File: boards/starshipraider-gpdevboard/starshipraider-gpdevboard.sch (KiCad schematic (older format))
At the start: 68 parts, among them J1 STARSHIPRAIDER_IOBOARD_MODULE, J2 GREENPAK_DEVKIT_HDR, P1 MMCX, P2 MMCX, P3 CONN_01X02, U1 74LVC1T45, U10 74LVC1T45, U11 74LVC1T45, U12 74LVC1T45, U13 74LVC1T45, U14 74LVC1T45, U15 74LVC1T45, U16 74LVC1T45, U17 74LVC1T45, U18 74LVC1T45, U19 TCA6424A, U2 74LVC1T45, U3 74LVC1T45, U4 74LVC1T45, U5 74LVC1T45, U6 74LVC1T45, U7 74LVC1T45, U8 74LVC1T45, U9 74LVC1T45

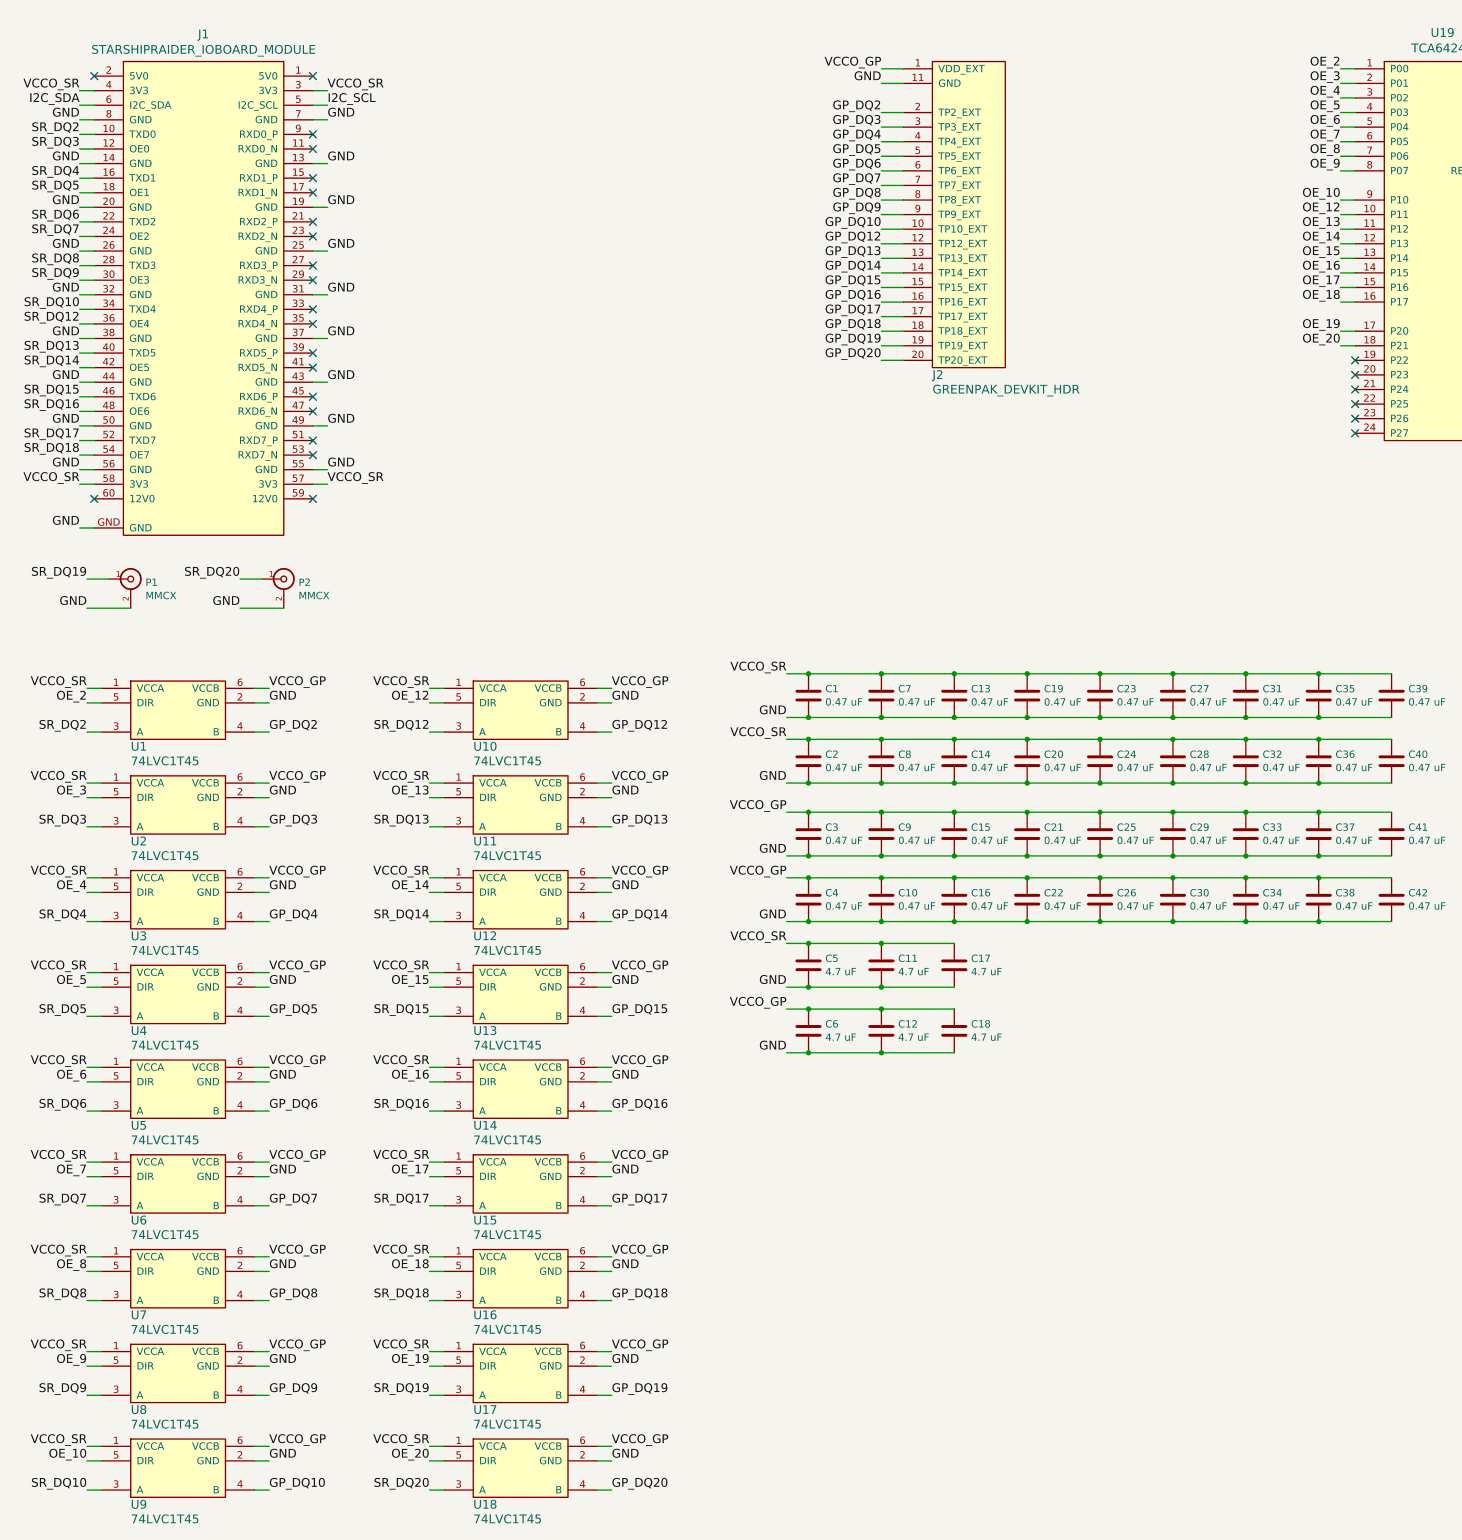
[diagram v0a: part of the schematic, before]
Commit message: Updating file: starshipraider-gpdevboard.kicad_pcb with current completely routed design
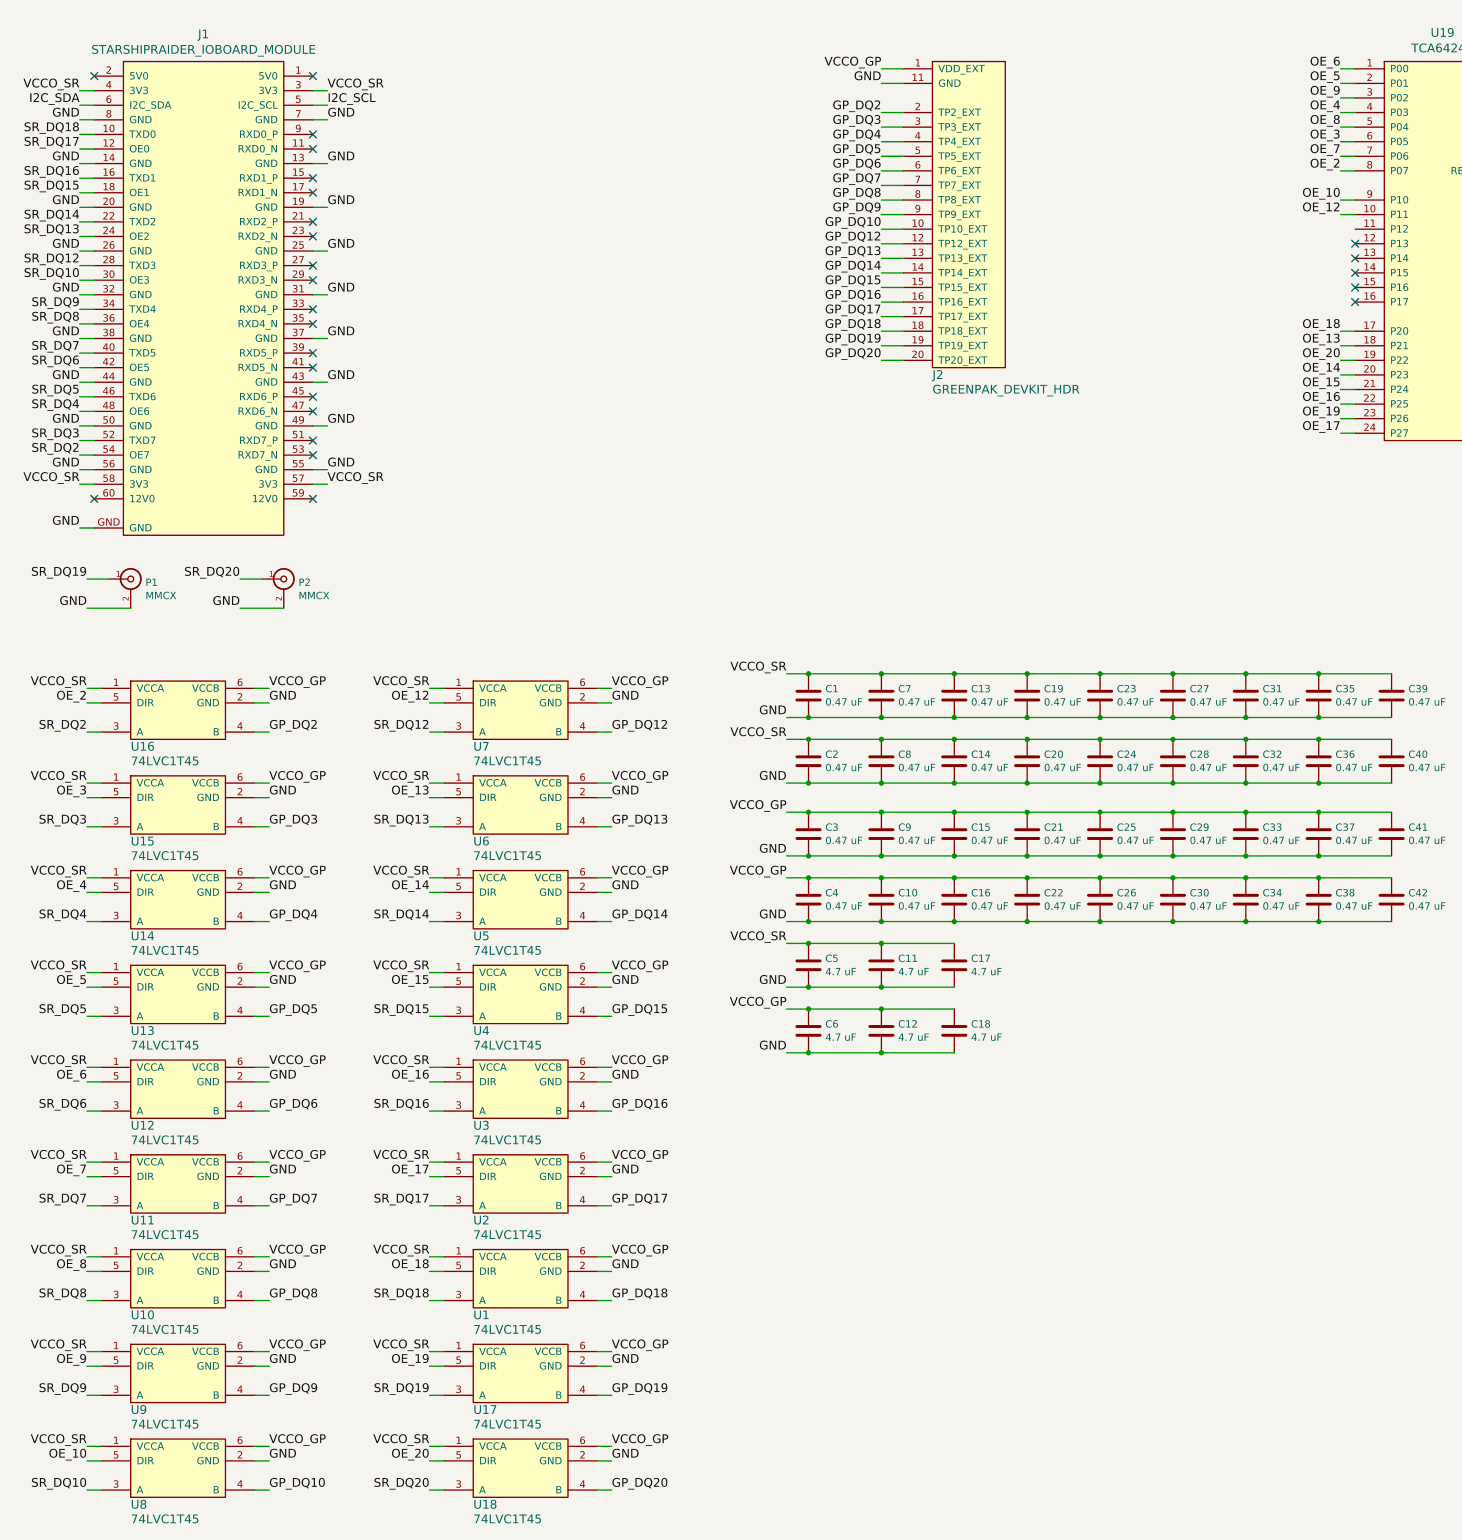
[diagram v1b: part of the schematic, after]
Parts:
- C1, C10, C13, C14, C15, C16, C19, C2, C20, C21, C22, C23, C24, C25, C26, C27, C28, C29, C3, C30, C31, C32, C33, C34, C35, C36, C37, C38, C39, C4, C40, C41, C42, C43, C7, C8, C9: footprint (none) -> azonenberg_pcb:EIA_0402_CAP_NOSILK
- C11, C12, C17, C18, C5, C6: footprint (none) -> azonenberg_pcb:EIA_0603_CAP_NOSILK
- J1: footprint (none) -> azonenberg_pcb:CONN_SAMTEC_QSH-030-01-L-D-A
- J2: footprint (none) -> azonenberg_pcb:CONN_HEADER_2.54MM_2x10_RA_FEMALE
- P1, P2: footprint (none) -> azonenberg_pcb:CONN_MMCX_LINX_CONNMMCX002SMD
- P3: footprint (none) -> azonenberg_pcb:CONN_HEADER_2.54MM_1x2
- R1: footprint (none) -> azonenberg_pcb:EIA_0402_RES_NOSILK
- U1, U10, U11, U12, U13, U14, U15, U16, U17, U18, U2, U3, U4, U5, U6, U7, U8, U9: footprint (none) -> azonenberg_pcb:SOT23_6
- U19: footprint (none) -> azonenberg_pcb:QFN_32_0.5MM_5x5MM
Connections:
- net GP_DQ10: now also U8.4 (B); no longer U9.4 (B)
- net GP_DQ12: now also U7.4 (B); no longer U10.4 (B)
- net GP_DQ13: now also U6.4 (B); no longer U11.4 (B)
- net GP_DQ14: now also U5.4 (B); no longer U12.4 (B)
- net GP_DQ15: now also U4.4 (B); no longer U13.4 (B)
- net GP_DQ16: now also U3.4 (B); no longer U14.4 (B)
- net GP_DQ17: now also U2.4 (B); no longer U15.4 (B)
- net GP_DQ18: now also U1.4 (B); no longer U16.4 (B)
- net GP_DQ2: now also U16.4 (B); no longer U1.4 (B)
- net GP_DQ3: now also U15.4 (B); no longer U2.4 (B)
- net GP_DQ4: now also U14.4 (B); no longer U3.4 (B)
- net GP_DQ5: now also U13.4 (B); no longer U4.4 (B)
- net GP_DQ6: now also U12.4 (B); no longer U5.4 (B)
- net GP_DQ7: now also U11.4 (B); no longer U6.4 (B)
- net GP_DQ8: now also U10.4 (B); no longer U7.4 (B)
- net GP_DQ9: now also U9.4 (B); no longer U8.4 (B)
- net OE_10: now also U8.5 (DIR); no longer U9.5 (DIR)
- net OE_12: now also U7.5 (DIR); no longer U10.5 (DIR)
- net OE_13: now also U19.18 (P21), U6.5 (DIR); no longer U11.5 (DIR), U19.11 (P12)
- net OE_14: now also U19.20 (P23), U5.5 (DIR); no longer U12.5 (DIR), U19.12 (P13)
- net OE_15: now also U19.21 (P24), U4.5 (DIR); no longer U13.5 (DIR), U19.13 (P14)
- net OE_16: now also U19.22 (P25), U3.5 (DIR); no longer U14.5 (DIR), U19.14 (P15)
- net OE_17: now also U19.24 (P27), U2.5 (DIR); no longer U15.5 (DIR), U19.15 (P16)
- net OE_18: now also U1.5 (DIR), U19.17 (P20); no longer U16.5 (DIR), U19.16 (P17)
- net OE_19: now also U19.23 (P26); no longer U19.17 (P20)
- net OE_2: now also U16.5 (DIR), U19.8 (P07); no longer U1.5 (DIR), U19.1 (P00)
- net OE_20: now also U19.19 (P22); no longer U19.18 (P21)
- net OE_3: now also U15.5 (DIR), U19.6 (P05); no longer U19.2 (P01), U2.5 (DIR)
- net OE_4: now also U14.5 (DIR), U19.4 (P03); no longer U19.3 (P02), U3.5 (DIR)
- net OE_5: now also U13.5 (DIR), U19.2 (P01); no longer U19.4 (P03), U4.5 (DIR)
- net OE_6: now also U12.5 (DIR), U19.1 (P00); no longer U19.5 (P04), U5.5 (DIR)
- net OE_7: now also U11.5 (DIR), U19.7 (P06); no longer U19.6 (P05), U6.5 (DIR)
- net OE_8: now also U10.5 (DIR), U19.5 (P04); no longer U19.7 (P06), U7.5 (DIR)
- net OE_9: now also U19.3 (P02), U9.5 (DIR); no longer U19.8 (P07), U8.5 (DIR)
- net SR_DQ10: now also J1.30 (OE3), U8.3 (A); no longer J1.34 (TXD4), U9.3 (A)
- net SR_DQ12: now also J1.28 (TXD3), U7.3 (A); no longer J1.36 (OE4), U10.3 (A)
- net SR_DQ13: now also J1.24 (OE2), U6.3 (A); no longer J1.40 (TXD5), U11.3 (A)
- net SR_DQ14: now also J1.22 (TXD2), U5.3 (A); no longer J1.42 (OE5), U12.3 (A)
- net SR_DQ15: now also J1.18 (OE1), U4.3 (A); no longer J1.46 (TXD6), U13.3 (A)
- net SR_DQ16: now also J1.16 (TXD1), U3.3 (A); no longer J1.48 (OE6), U14.3 (A)
- net SR_DQ17: now also J1.12 (OE0), U2.3 (A); no longer J1.52 (TXD7), U15.3 (A)
- net SR_DQ18: now also J1.10 (TXD0), U1.3 (A); no longer J1.54 (OE7), U16.3 (A)
- net SR_DQ2: now also J1.54 (OE7), U16.3 (A); no longer J1.10 (TXD0), U1.3 (A)
- net SR_DQ3: now also J1.52 (TXD7), U15.3 (A); no longer J1.12 (OE0), U2.3 (A)
- net SR_DQ4: now also J1.48 (OE6), U14.3 (A); no longer J1.16 (TXD1), U3.3 (A)
- net SR_DQ5: now also J1.46 (TXD6), U13.3 (A); no longer J1.18 (OE1), U4.3 (A)
- net SR_DQ6: now also J1.42 (OE5), U12.3 (A); no longer J1.22 (TXD2), U5.3 (A)
- net SR_DQ7: now also J1.40 (TXD5), U11.3 (A); no longer J1.24 (OE2), U6.3 (A)
- net SR_DQ8: now also J1.36 (OE4), U10.3 (A); no longer J1.28 (TXD3), U7.3 (A)
- net SR_DQ9: now also J1.34 (TXD4), U9.3 (A); no longer J1.30 (OE3), U8.3 (A)
- no-connect marks 26 -> 25
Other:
- moved on the sheet: U1, U10, U11, U12, U13, U14, U15, U16, U2, U3, U4, U5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
